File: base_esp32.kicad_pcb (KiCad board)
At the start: 2 copper layers, 100 x 100 mm, 77 parts, among them J1 Input Source, J10 H_IO15_OUT, J11 H_IO32_OUT, J12 H_IO02_OUT, J13 H_IO04_OUT, J14 H_5V, J15 S_5V, J16 H_3V3_1, J17 H_IO34, J18 H_IO35, J19 H_IO36, J2 BYPASS SRC 5V, J20 H_IO39, J21 S_3V3_1, J22 H_3V3_2, J23 H_KEYPAD, J24 H_I2C, J25 H_SPI, J26 TX_RX, J27 S_3V3_2, J28 H_GND, J29 S_KEYPAD, J3 BYPASS SRC 3V3, J30 S_I2C, J31 S_SPI, J32 S_GND, J33 H_Src Board, J4 H_IO33, J5 H_IO15, J6 H_IO32, J7 H_IO02, J8 H_IO04, J9 H_IO33_OUT, SW1 INPUT_D1, SW2 INPUT_D2, SW3 SW_DIP_INPUTS, SW4 ENABLE, SW5 SW_DIP_KEYPAD, SW6 Selector Input 1, SW7 Selector Input 2, SW8 BOOT, U1 LM7805_TO220, U2 AMS1117, U3 AMS1117, U4 ESP32-DevKitC

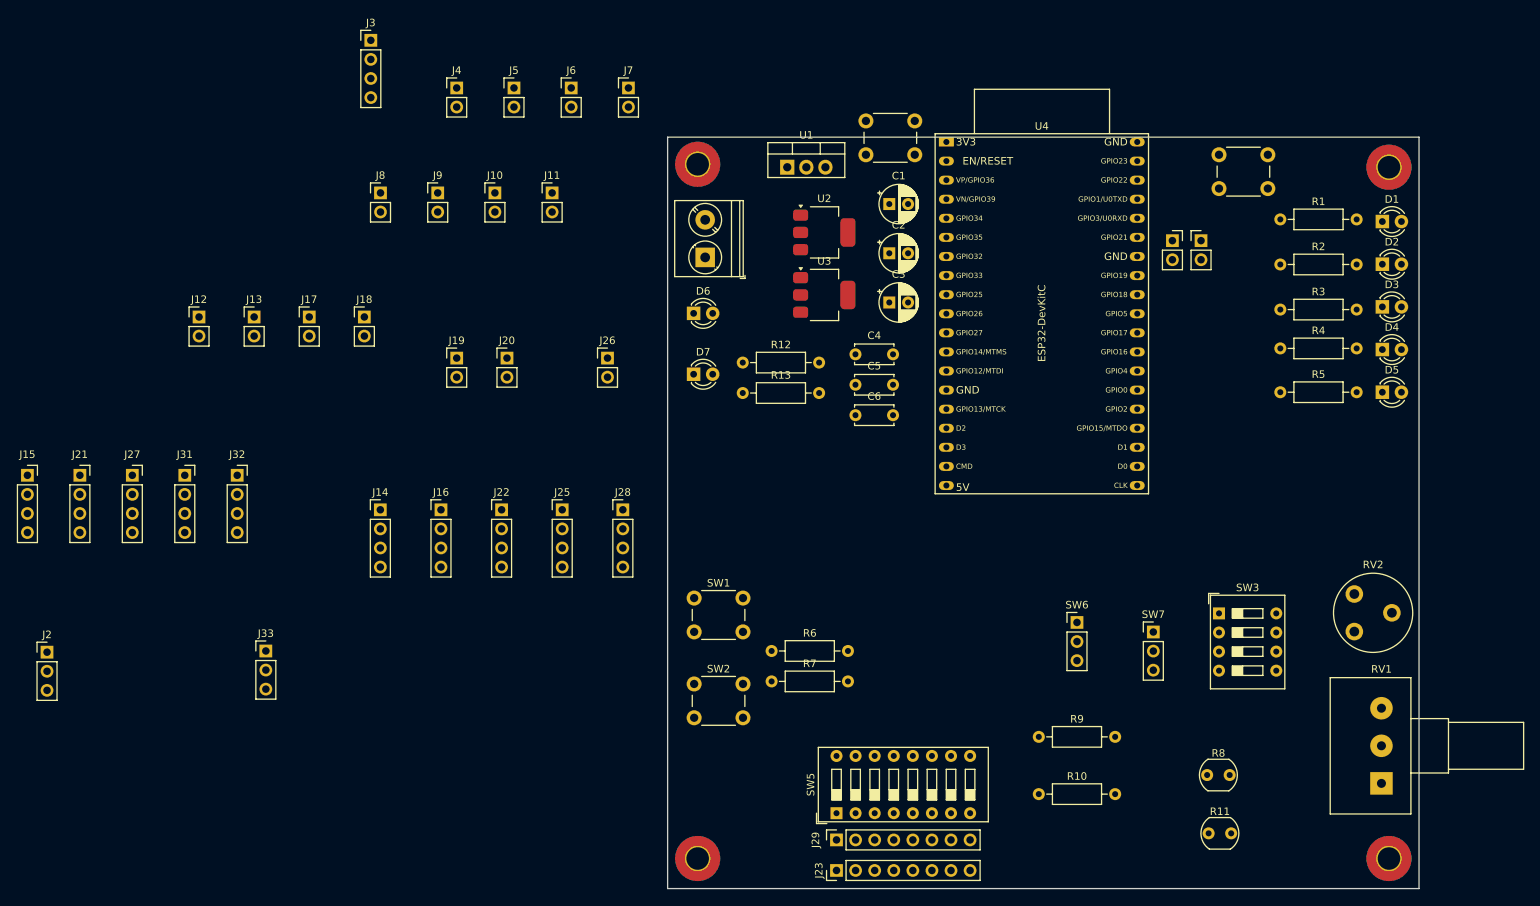
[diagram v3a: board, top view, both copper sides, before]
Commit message: add: some components to schematic
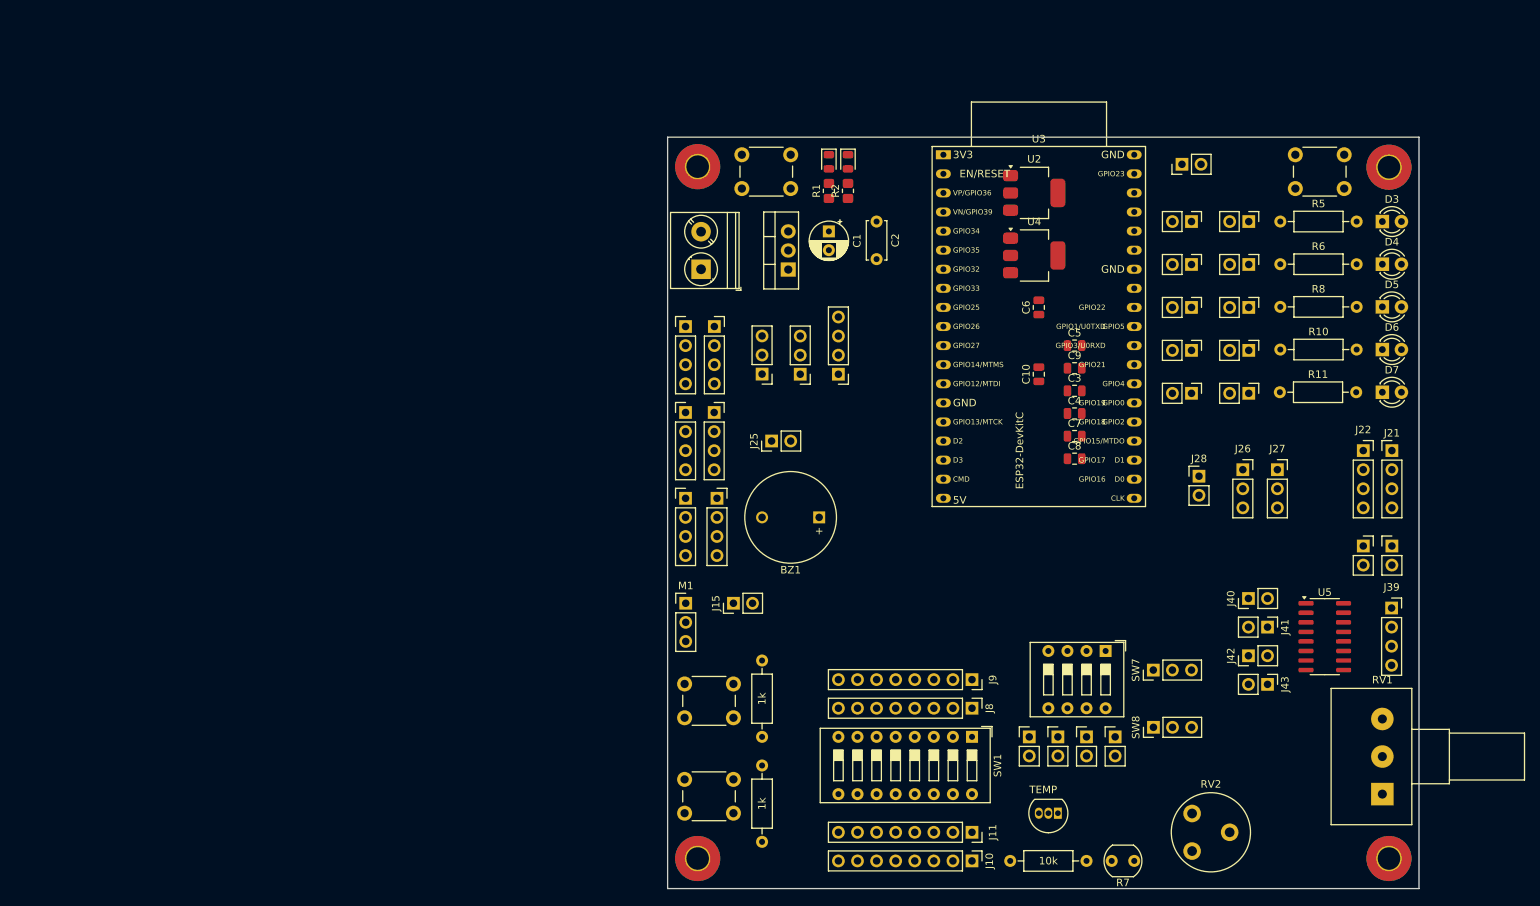
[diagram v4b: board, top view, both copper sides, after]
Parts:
- removed the C1 at (132.5, 59.9)
- removed the C2 at (132.5, 66.5)
- removed the J16 at (72.8, 100.6)
- removed the J21 at (24.8, 96.0)
- removed the R10 at (152.4, 138.4)
- removed the R11 at (175.0, 143.7)
- added BZ1: Buzzer, Buzzer_Beeper:MagneticBuzzer_ProSignal_ABI-010-RC, F.Cu at (123.2, 101.6)
- added C3: 100nF, Capacitor_SMD:C_0805_2012Metric, F.Cu at (157.2, 84.8)
- added C4: 100nF, Capacitor_SMD:C_0805_2012Metric, F.Cu at (157.2, 87.8)
- added C5: 10nF, Capacitor_SMD:C_0805_2012Metric, F.Cu at (157.2, 78.7)
- added C7: 100nF, Capacitor_SMD:C_0805_2012Metric, F.Cu at (157.2, 90.8)
- added C8: 100nF, Capacitor_SMD:C_0805_2012Metric, F.Cu at (157.2, 93.8)
- added C9: 10uF, Capacitor_SMD:C_0805_2012Metric, F.Cu at (157.2, 81.8)
- added J15: H_SERVO, Connector_PinHeader_2.54mm:PinHeader_1x02_P2.54mm_Vertical, F.Cu at (111.8, 113.0)
- added J25: H_BUZZER, Connector_PinHeader_2.54mm:PinHeader_1x02_P2.54mm_Vertical, F.Cu at (116.8, 91.4)
- added J26: DTH11_V1, Connector_PinSocket_2.54mm:PinSocket_1x03_P2.54mm_Vertical, F.Cu at (179.6, 95.2)
- added J27: DTH11_V2, Connector_PinSocket_2.54mm:PinSocket_1x03_P2.54mm_Vertical, F.Cu at (184.2, 95.2)
- added J28: H_DTH11, Connector_PinHeader_2.54mm:PinHeader_1x02_P2.54mm_Vertical, F.Cu at (173.7, 96.1)
- added J39: MOTOR, Connector_PinSocket_2.54mm:PinSocket_1x04_P2.54mm_Vertical, F.Cu at (199.3, 113.7)
- added J40: H_INA1, Connector_PinHeader_2.54mm:PinHeader_1x02_P2.54mm_Vertical, F.Cu at (180.3, 112.4)
- added J41: H_INB1, Connector_PinHeader_2.54mm:PinHeader_1x02_P2.54mm_Vertical, F.Cu at (182.8, 116.2)
- added J42: H_INA2, Connector_PinHeader_2.54mm:PinHeader_1x02_P2.54mm_Vertical, F.Cu at (180.3, 120.0)
- added J43: H_INB2, Connector_PinHeader_2.54mm:PinHeader_1x02_P2.54mm_Vertical, F.Cu at (182.8, 123.8)
- added J8: H_IO, Connector_PinHeader_2.54mm:PinHeader_1x08_P2.54mm_Vertical, F.Cu at (143.5, 127.0)
- added J9: S_IO, Connector_PinSocket_2.54mm:PinSocket_1x08_P2.54mm_Vertical, F.Cu at (143.5, 123.2)
- added M1: Servo, Connector_PinHeader_2.54mm:PinHeader_1x03_P2.54mm_Vertical, F.Cu at (105.4, 113.0)
- added U5: MX1508, Package_SO:SOP-16_3.9x9.9mm_P1.27mm, F.Cu at (190.5, 117.5)
- added U6: LM35-LP, Package_TO_SOT_THT:TO-92_Inline, F.Cu at (154.9, 141.0)
- C10: renamed from C5; value 0.1uF -> 100nF; footprint Capacitor_THT:C_Disc_D5.0mm_W2.5mm_P5.00mm -> Capacitor_SMD:C_0805_2012Metric
- C6: renamed from C4; value 0.1uF -> 100nF; footprint Capacitor_THT:C_Disc_D5.0mm_W2.5mm_P5.00mm -> Capacitor_SMD:C_0805_2012Metric
- D1: renamed from D6; footprint LED_THT:LED_D3.0mm -> LED_SMD:LED_0805_2012Metric
- D2: renamed from D7; footprint LED_THT:LED_D3.0mm -> LED_SMD:LED_0805_2012Metric
- R1: renamed from R12; footprint Resistor_THT:R_Axial_DIN0207_L6.3mm_D2.5mm_P10.16mm_Horizontal -> Resistor_SMD:R_0805_2012Metric_Pad1.20x1.40mm_HandSolder
- R2: renamed from R13; footprint Resistor_THT:R_Axial_DIN0207_L6.3mm_D2.5mm_P10.16mm_Horizontal -> Resistor_SMD:R_0805_2012Metric_Pad1.20x1.40mm_HandSolder
- moved J22 156.9 mm to (195.6, 92.7)
- moved J36 132.2 mm to (172.7, 79.4), turned to -90 degrees
- moved J38 125.2 mm to (172.7, 85.1), turned to -90 degrees
- moved J14 120.9 mm to (162.6, 130.8)
- moved J37 118.6 mm to (180.3, 85.1), turned to -90 degrees
- moved J19 111.2 mm to (158.8, 130.8)
- moved J21 110.7 mm to (199.4, 92.7)
- moved J30 106.9 mm to (180.3, 62.2), turned to -90 degrees
- moved J12 102.1 mm to (115.6, 82.5), turned to 180 degrees
- moved J31 100.6 mm to (180.3, 67.9), turned to -90 degrees
- moved J29 100.4 mm to (172.7, 62.2), turned to -90 degrees
- moved J33 94.8 mm to (180.3, 73.7), turned to -90 degrees
- moved J20 94.6 mm to (154.9, 130.8)
- moved J32 93.2 mm to (172.7, 67.9), turned to -90 degrees
- moved J2 91.8 mm to (109.2, 87.6)
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- renumbered C3 to C1, C6 to C2, D1 to D3, D2 to D4, D3 to D5, D4 to D6, D5 to D7, J14 to J1, J23 to J10, J29 to J11, J2 to J12, J3 to J13, J17 to J14, J33 to J16, J24 to J17, J30 to J18, J18 to J19, J15 to J2, J19 to J20, J25 to J21, J31 to J22, J20 to J23, J26 to J24, J9 to J29, J22 to J3, J4 to J30, J5 to J31, J10 to J32, J6 to J33, J11 to J34, J7 to J35, J12 to J36, J8 to J37, J13 to J38, J27 to J4, J28 to J5, J32 to J6, J1 to J7, R4 to R10, R5 to R11, R6 to R3, R7 to R4, R1 to R5, R2 to R6, R8 to R7, R3 to R8, SW5 to SW1, SW4 to SW2, SW8 to SW3, SW1 to SW4, SW3 to SW5, SW2 to SW6, SW6 to SW7, SW7 to SW8, U4 to U3, U3 to U4
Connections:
- net /IO32 renamed /BUZZER
- SW8 pad 1: /LDR_2 -> /LM35
- U2 pad 3: VCC -> +5V
- U4 pad 3: VCC -> +5V
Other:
- board text added: "TEMP"

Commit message: rm: header
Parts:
- added SW2: SW_DIP_KEYPAD_2, Button_Switch_THT:SW_DIP_SPSTx04_Slide_9.78x12.34mm_W7.62mm_P2.54mm, F.Cu at (130.8, 131.5)
- SW1: value SW_DIP_KEYPAD -> SW_DIP_KEYPAD_1; footprint Button_Switch_THT:SW_DIP_SPSTx08_Slide_9.78x22.5mm_W7.62mm_P2.54mm -> Button_Switch_THT:SW_DIP_SPSTx04_Slide_9.78x12.34mm_W7.62mm_P2.54mm
- moved SW4 73.0 mm to (120.1, 57.5)
- moved SW3 71.2 mm to (184.1, 53.0)
- moved U3 51.6 mm to (164.5, 98.6), turned to 180 degrees
- moved J22 44.0 mm to (153.0, 112.4), turned to -90 degrees
- moved C5 40.6 mm to (116.8, 83.8)
- moved C6 38.2 mm to (116.8, 87.6), turned to 0 degrees
- moved U2 37.6 mm to (119.4, 77.5)
- moved C7 35.9 mm to (121.9, 83.8)
- moved C8 35.8 mm to (121.9, 87.6)
- moved U6 30.3 mm to (184.8, 146.4), turned to 0 degrees
- moved C3 28.9 mm to (128.3, 83.8)
- moved C4 28.9 mm to (128.3, 87.6)
- moved R7 26.1 mm to (167.0, 121.3), turned to 90 degrees
- moved C9 23.9 mm to (133.3, 83.8), turned to 180 degrees
- moved U4 23.6 mm to (130.8, 77.5)
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- renumbered J40 to J14, J41 to J15, J15 to J16, J14 to J17, J17 to J18, J18 to J19, J19 to J20, J42 to J21, J16 to J22, J43 to J23, J20 to J24, J21 to J25, J22 to J26, J23 to J27, J24 to J28, J26 to J29, J27 to J30, J28 to J31, J25 to J32, J29 to J33, J30 to J34, J39 to J35, J31 to J36, J32 to J37, J33 to J38, J34 to J39, J35 to J40, J36 to J41, J37 to J42, J38 to J43, SW2 to SW3, SW3 to SW4, SW4 to SW5, SW5 to SW6, SW6 to SW7, SW7 to SW8, SW8 to SW9
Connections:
- J22 pad 2: GND -> VCC
- J22 pad 3: VCC3 -> VCC
- SW1 pad 5: /IO16 -> /IO27_IN
- SW1 pad 6: /IO17 -> /IO14_IN
- SW1 pad 7: /IO25 -> /IO12_IN
- SW1 pad 8: /IO26 -> /IO13_IN
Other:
- board text added: "1"
- board text added: "3V3"
- board text added: "5V"
- board text added: "DATA"
- board text added: "DTH11"
- board text added: "GND"
- board text added: "I2C"
- board text added: "IO02"
- board text added: "IO12"
- board text added: "IO13"
- board text added: "IO14"
- board text added: "IO16"
- board text added: "IO17"
- board text added: "IO25"
- board text added: "IO26"
- board text added: "IO27"
- board text added: "IO32-BZ"
- board text added: "IO34/A"
- board text added: "IO35/A"
- board text added: "IO36"
- board text added: "IO39"
- board text added: "KEYBOARD"
- board text added: "LM35 TEMP"
- board text added: "PWM"
- board text added: "RX"
- board text added: "SERVO"
- board text added: "SERVO-IO04"
- board text added: "SPI"
- board text added: "TX"
- board text removed: "TEMP"

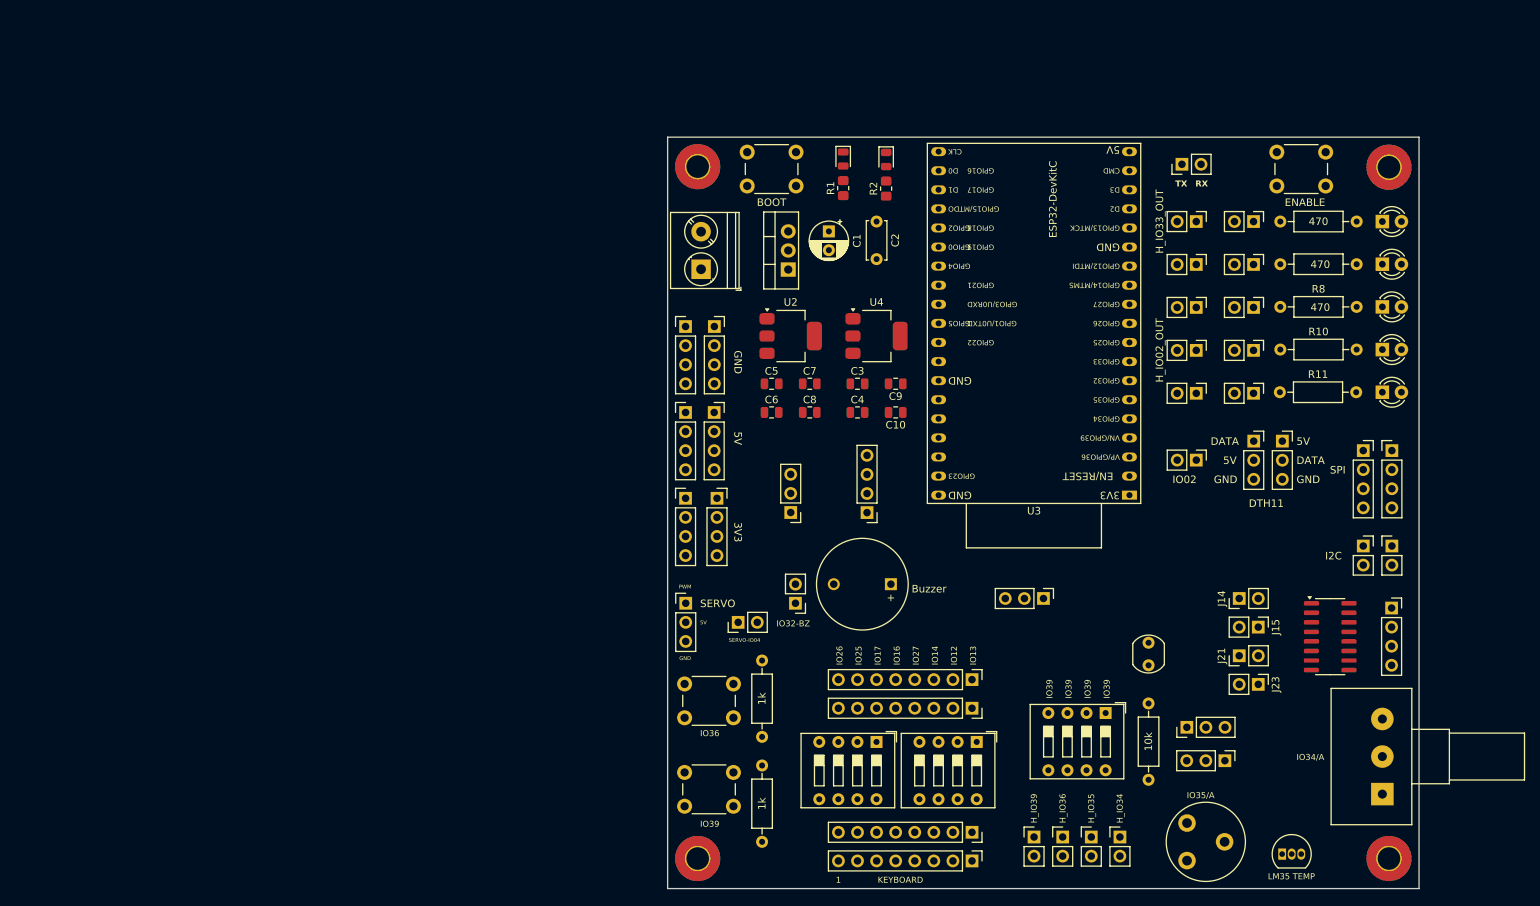
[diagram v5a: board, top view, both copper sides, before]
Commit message: add: ultrasonic
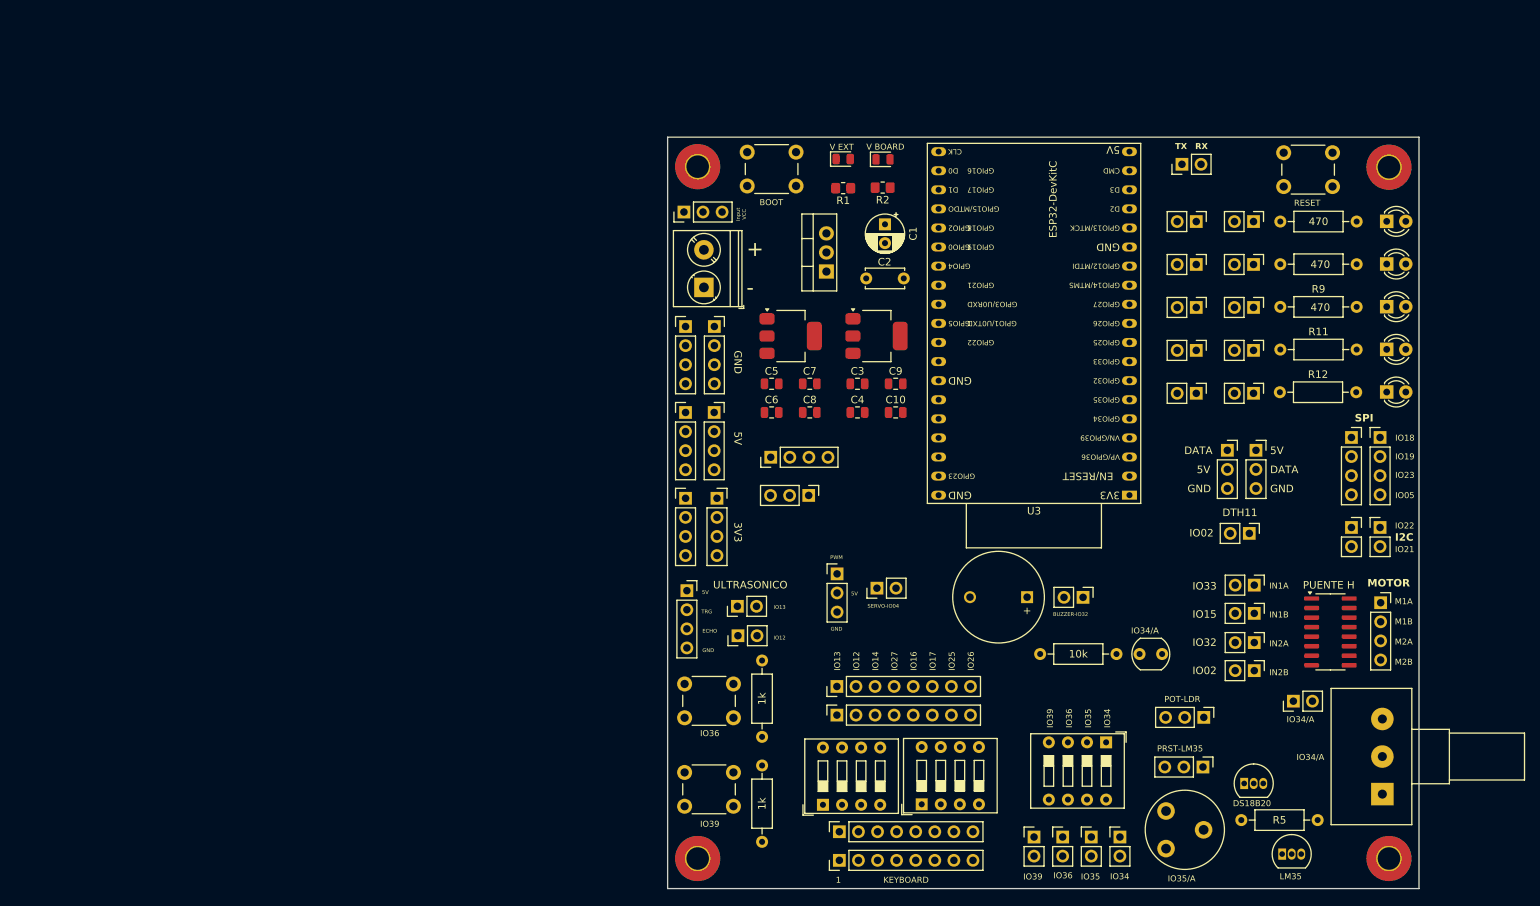
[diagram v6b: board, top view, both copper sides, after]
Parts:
- added J31: H_DS18B, Connector_PinHeader_2.54mm:PinHeader_1x02_P2.54mm_Vertical, F.Cu at (186.3, 126.1)
- added J35: H_TRIGGER, Connector_PinHeader_2.54mm:PinHeader_1x02_P2.54mm_Vertical, F.Cu at (112.3, 113.4)
- added J38: ULTRASONIC, Connector_PinSocket_2.54mm:PinSocket_1x04_P2.54mm_Vertical, F.Cu at (105.6, 111.4)
- added J41: H_ECHO, Connector_PinHeader_2.54mm:PinHeader_1x02_P2.54mm_Vertical, F.Cu at (112.4, 117.3)
- added R5: 4k7, Resistor_THT:R_Axial_DIN0207_L6.3mm_D2.5mm_P10.16mm_Horizontal, F.Cu at (179.3, 141.9)
- added U6: DS18B20, Package_TO_SOT_THT:TO-92_Inline, F.Cu at (179.7, 137.0)
- J1: renamed from J22; value H_Src Board -> H_Src_raw
- moved J1 70.3 mm to (105.2, 61.0), turned to 90 degrees
- moved J17 38.3 mm to (158.3, 112.2), turned to -90 degrees
- moved SW1 22.1 mm to (123.7, 139.9), turned to 90 degrees
- moved R10 22.1 mm to (152.6, 119.8), turned to 0 degrees
- moved M1 20.5 mm to (125.6, 109.1)
- moved J15 19.0 mm to (130.9, 111.0)
- moved BZ1 18.2 mm to (150.8, 112.2)
- moved J10 18.0 mm to (125.5, 127.9), turned to 90 degrees
- moved J9 18.0 mm to (125.5, 124.1), turned to 90 degrees
- moved J11 17.7 mm to (125.9, 147.2), turned to 90 degrees
- moved J12 17.7 mm to (125.9, 143.4), turned to 90 degrees
- moved J14 14.8 mm to (116.7, 93.6), turned to 90 degrees
- moved J30 12.0 mm to (180.4, 103.7)
- moved SW2 10.2 mm to (136.8, 139.8), turned to 90 degrees
- moved C2 7.69 mm to (129.4, 69.8), turned to 0 degrees
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- renumbered J9 to J10, J10 to J11, J11 to J12, J12 to J13, J13 to J14, J16 to J15, J14 to J16, J32 to J17, J15 to J18, J17 to J19, J1 to J2, J18 to J20, J19 to J21, J20 to J22, J21 to J23, J23 to J24, J24 to J25, J25 to J26, J26 to J27, J29 to J28, J30 to J29, J2 to J3, J31 to J30, J27 to J32, J28 to J33, J35 to J34, J33 to J36, J34 to J37, J36 to J39, J3 to J4, J37 to J40, J38 to J42, J39 to J43, J40 to J44, J41 to J45, J42 to J46, J43 to J47, J4 to J5, J5 to J6, J6 to J7, J7 to J8, J8 to J9, R9 to R10, R10 to R11, R11 to R12, R5 to R6, R6 to R7, R7 to R8, R8 to R9, U6 to U7
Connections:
- net /IO15 renamed /DS18B
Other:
- board text added: "+"
- board text added: "-"
- board text added: "BOOT"
- board text added: "BUZZER-IO32"
- board text added: "DS18B20"
- board text added: "ECHO"
- board text added: "IN1A"
- board text added: "IN1B"
- board text added: "IN2A"
- board text added: "IN2B"
- board text added: "IO05"
- board text added: "IO15"
- board text added: "IO18"
- board text added: "IO19"
- board text added: "IO21"
- board text added: "IO22"
- board text added: "IO23"
- board text added: "IO32"
- board text added: "IO33"
- board text added: "IO34"
- board text added: "IO35"
- board text added: "Input VCC"
- board text added: "LM35"
- board text added: "M1A"
- board text added: "M1B"
- board text added: "M2A"
- board text added: "M2B"
- board text added: "MOTOR"
- board text added: "POT-LDR"
- board text added: "PRST-LM35"
- board text added: "PUENTE H"
- board text added: "RESET"
- board text added: "TRG"
- board text added: "ULTRASONICO"
- board text added: "V BOARD"
- board text added: "V EXT"
- board text removed: "IO32-BZ"
- board text removed: "LM35 TEMP"
